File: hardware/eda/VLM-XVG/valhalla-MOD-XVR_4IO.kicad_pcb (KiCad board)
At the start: 2 copper layers, 206.2 x 99.6 mm, 131 parts, among them J1 POWER, J14 GLM_F, J15 GLM_F, J16 GLM_F, J17 GLM_F, J18 GLM_B, J19 GLM_B, J2 FIELD, J20 GLM_B, J21 GLM_B, J22 WDM_I, J23 WDM_I, J24 TM, J25 FIM_I, J26 FIM_I, J27 FIM_I, J28 FIM_I, J29 WDM_I, J3 GPIO, J30 FIM_I, J31 TM_0, J32 TM_1, J33 FIM_I, J34 WDM_E, J35 WDM_E, J36 WDM_E, J37 FIM_I, J38 FIM_I, J39 FIM_I, J4 FIM_E, J40 FIM_I, J5 FIM_E, J6 FIM_E, J7 FIM_E, J8 FIM_E, Q1 IRLZ44N, Q2 IRLZ44N, Q3 2N3904, Q4 2N3904, Q5 2N3906, Q6 2N3906, U1 4N35, U2 4N35, U3 74HC14, U4 4N35, U5 4N35, U6 74HC74, U8 74HC123, U9 74HC04

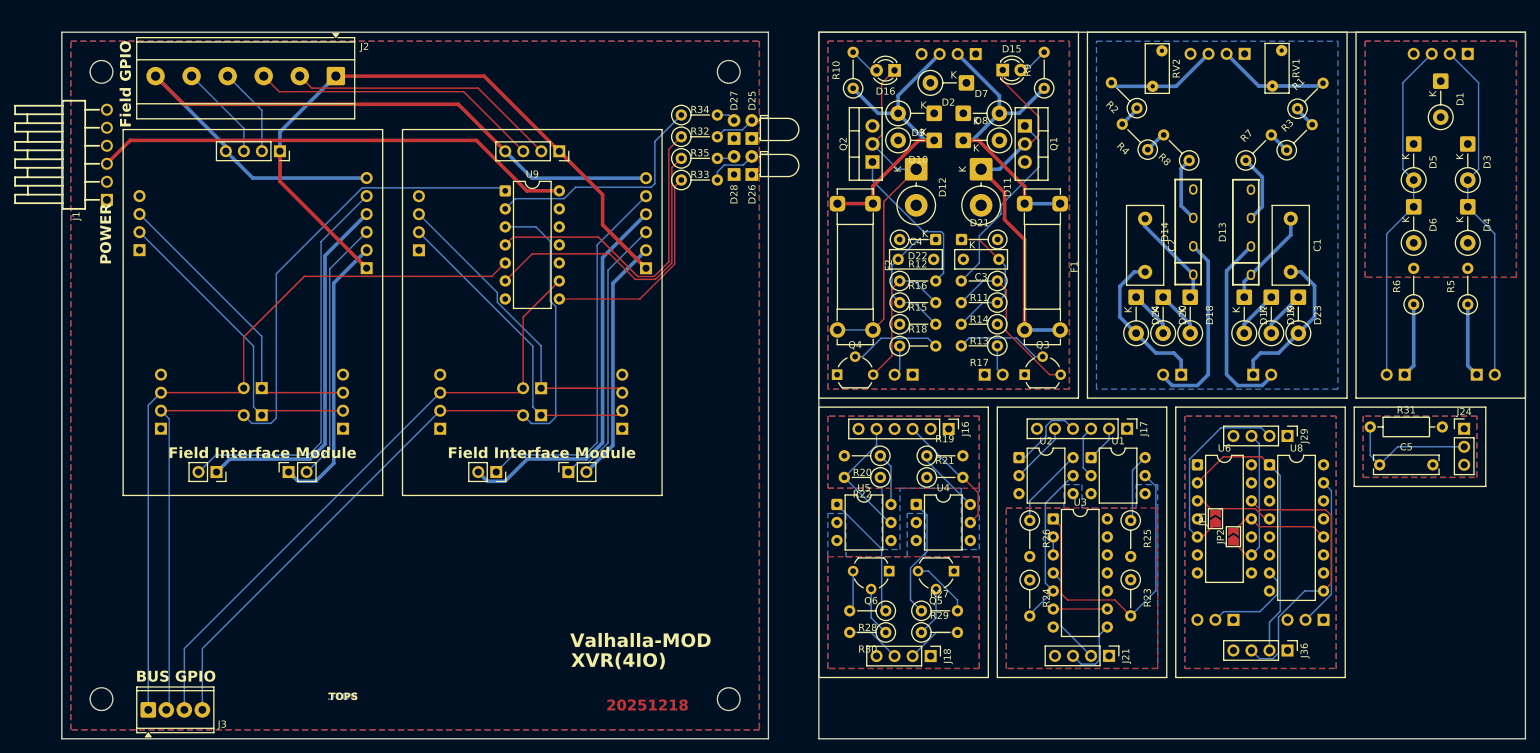
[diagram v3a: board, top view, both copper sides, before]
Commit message: UPDATE: progess on MOD-XVR(4IO)
 - fixed the other 1/2 of loop ampacity issues on power GPO FIM
 - revised clearance/creepage solution for GPI FIM
 - silkscreen references pass complete for all three FIMs
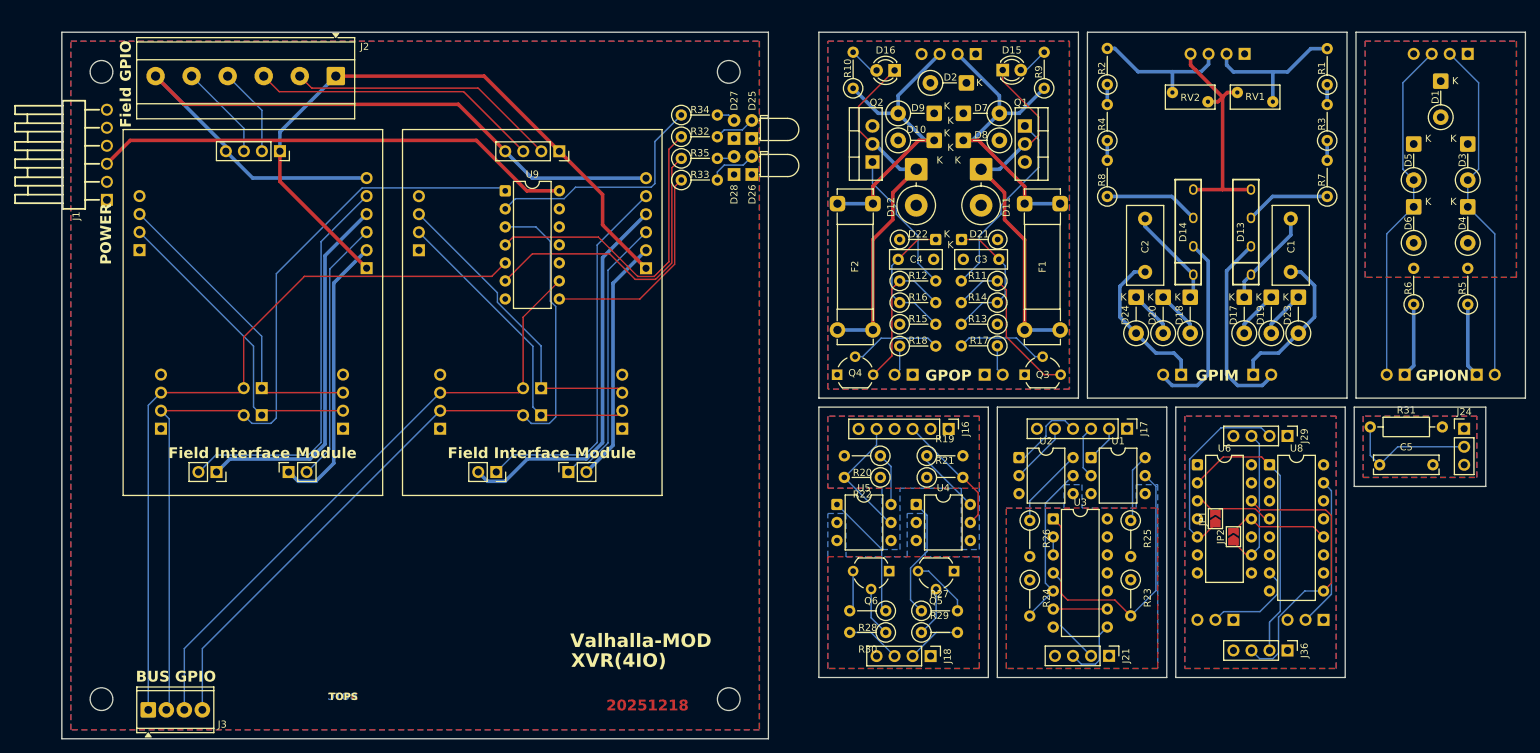
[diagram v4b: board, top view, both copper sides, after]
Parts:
- moved R8 12.6 mm to (172.7, 48.5), turned to 90 degrees
- moved R7 12.5 mm to (203.7, 48.5), turned to 90 degrees
- moved R3 5.86 mm to (203.7, 40.7), turned to 90 degrees
- moved R4 5.84 mm to (172.7, 40.7), turned to 90 degrees
- moved R1 5.38 mm to (203.7, 32.8), turned to 90 degrees
- moved R2 5.35 mm to (172.7, 32.8), turned to 90 degrees
- moved RV2 2.92 mm to (181.9, 33.9), turned to 0 degrees
- moved RV1 2.21 mm to (196.0, 35.2), turned to 180 degrees
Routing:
- net /IXVR_GND: track 0.00 -> 33.8 mm
- net Net-(J8-Pin_2): track 15.6 -> 21.7 mm
- net Net-(J8-Pin_3): track 15.8 -> 20.5 mm
- net Net-(D14-Pad3): track 9.27 -> 13.4 mm
- net Net-(Q2-G): track 22.8 -> 20.5 mm
- net Net-(D13-Pad3): track 9.74 -> 12.0 mm
- net Net-(D12-K): track 49.5 -> 51.1 mm
- removed copper zone on B.Cu, net /IXVR_GND
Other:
- outline, holes or cut-outs redrawn
- board text added: "GPIM"
- board text added: "GPION"
- board text added: "GPOP"

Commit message: UPDATE: finished silkscreen on MOD-XVR(4IO)
  - finalized mechanical details of Timing Module interface to
    Watchdog/Debouncer module
  - finalized silkscreen of all daughtercards
  - overhanging parts on main board still need their silkscreen clipped
    to the board edge.
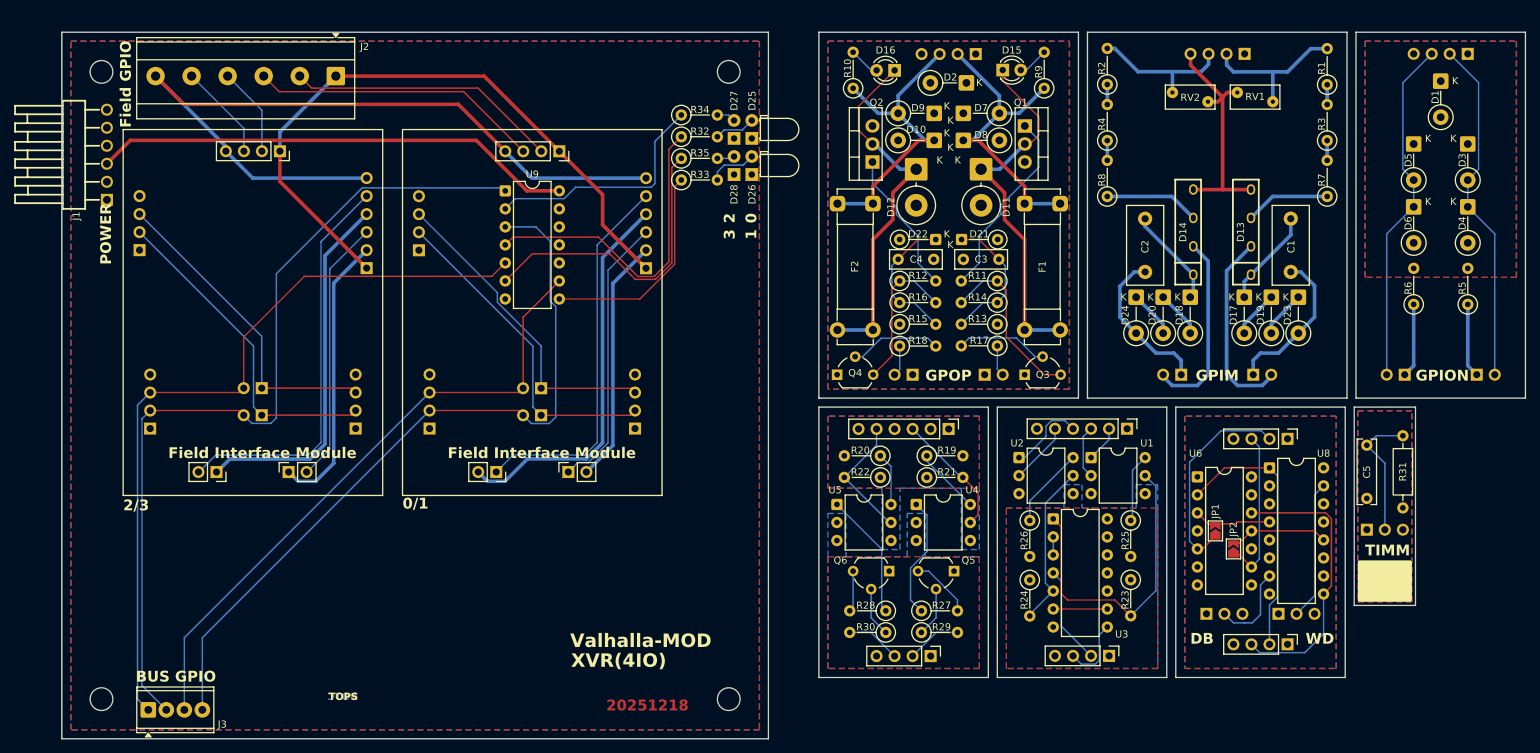
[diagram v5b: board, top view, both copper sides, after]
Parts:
- J24: footprint Connector_PinHeader_2.54mm:PinHeader_1x03_P2.54mm_Vertical -> Connector_PinHeader_2.54mm:PinHeader_1x03_P2.54mm_Horizontal; moved to B.Cu
- J31, J32: footprint Connector_PinSocket_2.54mm:PinSocket_1x03_P2.54mm_Vertical -> Connector_PinSocket_2.54mm:PinSocket_1x03_P2.54mm_Horizontal
- moved J24 19.8 mm to (209.3, 95.5), turned to -90 degrees
- moved J31 6.41 mm to (196.8, 107.4), turned to -90 degrees
- moved R31 4.77 mm to (214.4, 82.3), turned to -90 degrees
- moved J32 3.90 mm to (186.7, 107.4), turned to -90 degrees
- moved C5 3.30 mm to (209.3, 83.6), turned to -90 degrees
- moved J22 1.80 mm to (106.2, 81.3)
- moved J23 1.78 mm to (66.8, 81.3)
- moved JP1 1.72 mm to (188.0, 95.7)
- moved JP2 1.72 mm to (190.5, 98.2)
- moved U6 1.70 mm to (185.4, 88.1)
- moved J35 1.52 mm to (37.8, 81.3)
- moved J34 1.50 mm to (77.2, 81.3)
- moved J36 0.86 mm to (198.1, 111.7)
- moved U8 0.43 mm to (195.6, 86.8)
- moved J29 0.41 mm to (198.1, 82.7)
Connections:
- J24 pad 1: /WDTM_DVCC -> /WDTM_DGND
- J24 pad 3: /WDTM_DGND -> /WDTM_DVCC
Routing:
- net /~{BGPIO_E_2}: track 117.9 -> 120.1 mm
- net /~{BGPIO_E_3}: track 105.8 -> 107.9 mm
- net Net-(J36-Pin_2): track 39.5 -> 37.5 mm
- net /~{BGPIO_I_0}: track 44.6 -> 46.5 mm
- net /~{BGPIO_I_1}: track 43.4 -> 45.2 mm
- net /~{BGPIO_I_2}: track 44.7 -> 46.4 mm
- net /~{BGPIO_I_3}: track 43.4 -> 45.2 mm
- net Net-(J31-Pin_2): track 21.3 -> 19.6 mm
- net Net-(J32-Pin_2): track 13.7 -> 12.2 mm
- net Net-(J29-Pin_3): track 21.0 -> 22.2 mm
- net Net-(J29-Pin_2): track 28.3 -> 29.5 mm
- net Net-(JP1-B): track 11.8 -> 10.7 mm
- net /~{BGPIO_E_0}: track 105.7 -> 106.6 mm
- net /~{BGPIO_E_1}: track 88.8 -> 89.7 mm
- net Net-(D15-A): track 4.34 -> 3.55 mm
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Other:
- outline, holes or cut-outs redrawn
- board text added: "0"
- board text added: "0/1"
- board text added: "1"
- board text added: "2"
- board text added: "2/3"
- board text added: "3"
- board text added: "DB"
- board text added: "GPIL"
- board text added: "GPOL"
- board text added: "INPUT"
- board text added: "OUTPUT"
- board text added: "TIMM"
- board text added: "Timing Module"
- board text added: "WD"
